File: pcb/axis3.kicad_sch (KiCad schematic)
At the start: 10 parts, among them J13 Mini v1.0 FEMALE sockets, J23 MOTOR PHASES male 1x3, J33 ENCODER JST-SH 6p, J43 MINI POWER: +12V / GND

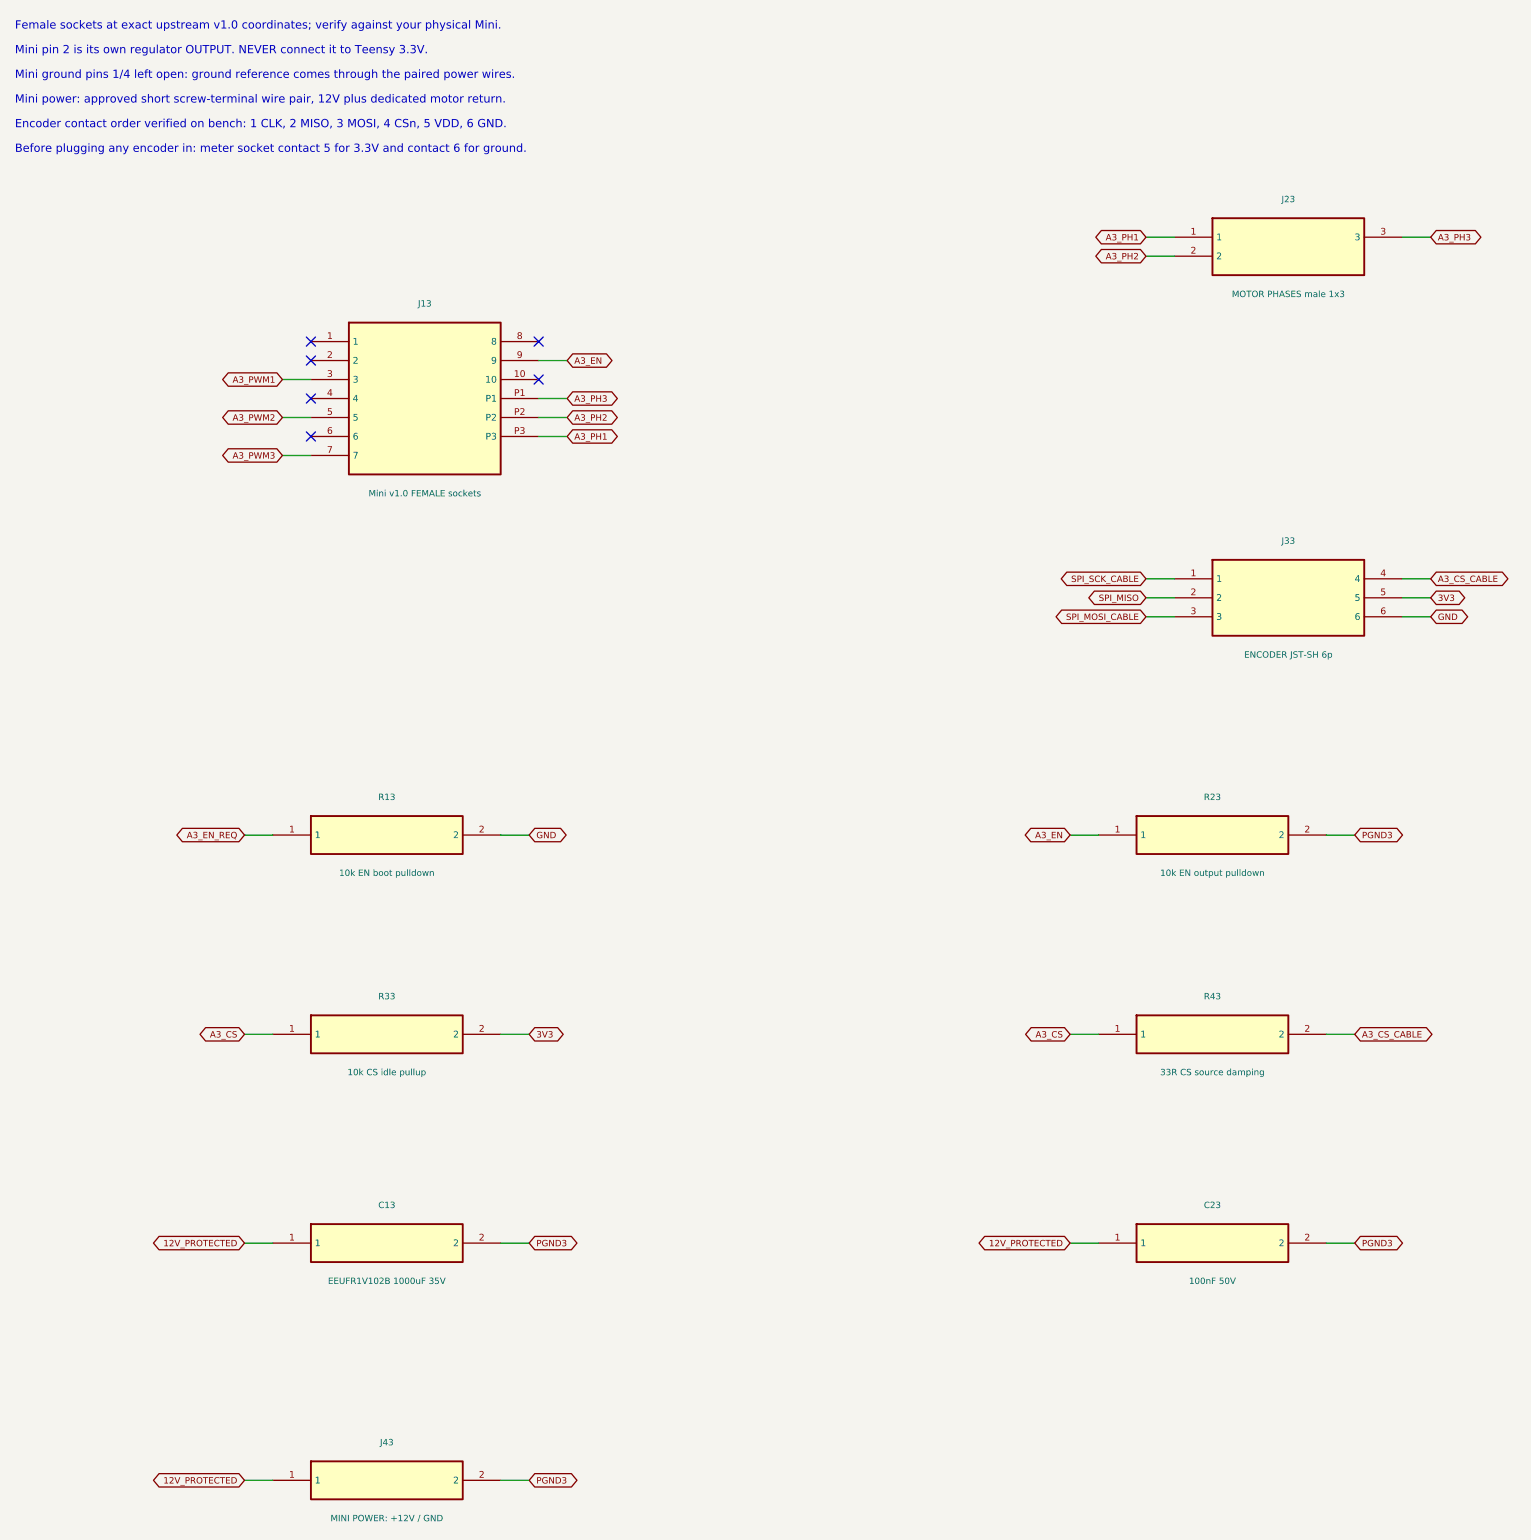
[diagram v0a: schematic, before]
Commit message: feat: finish through-hole six-axis carrier review design
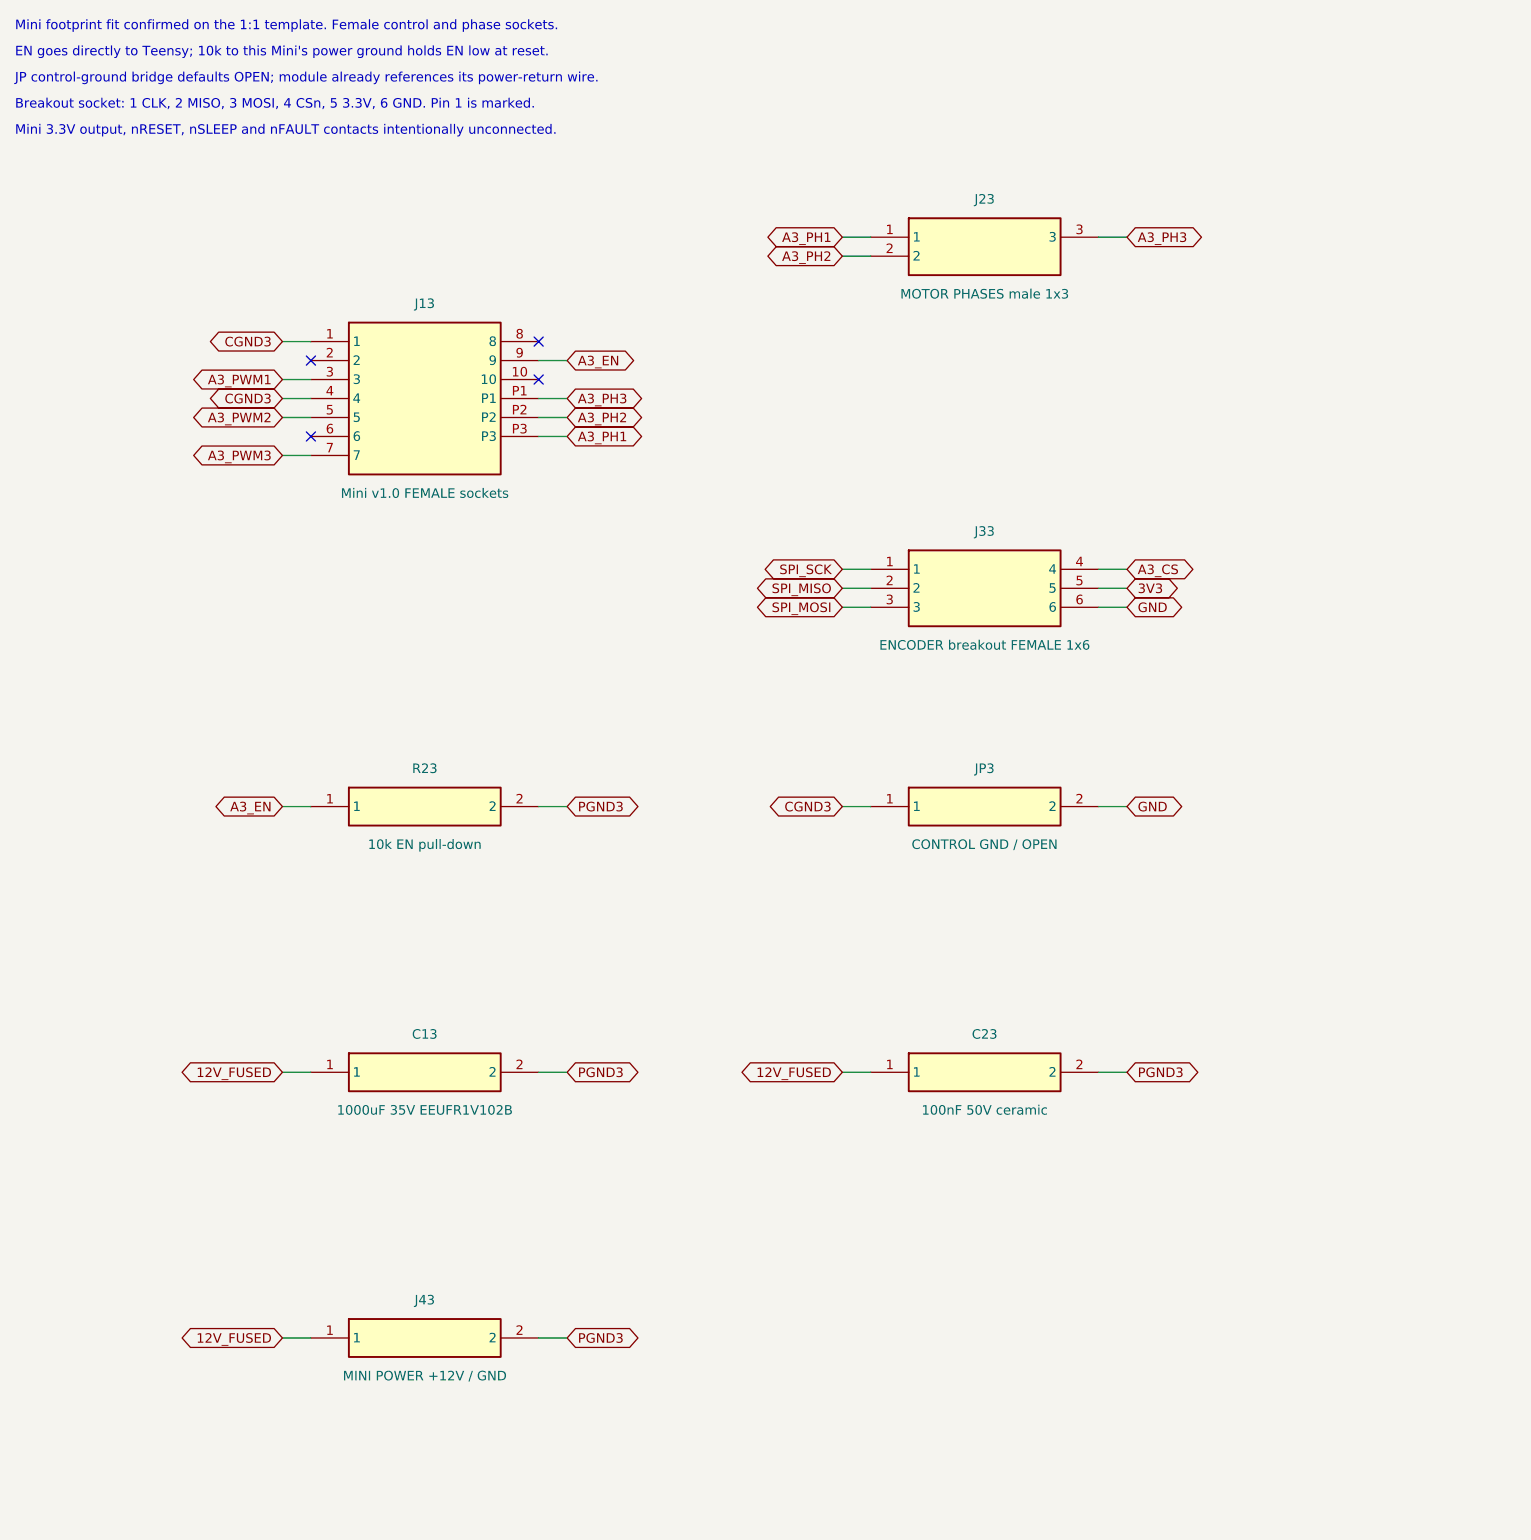
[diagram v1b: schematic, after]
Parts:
- removed R13: 10k EN boot pulldown, Resistor_SMD:R_0603_1608Metric, symbol TrueSkate:R13
- removed R33: 10k CS idle pullup, Resistor_SMD:R_0603_1608Metric, symbol TrueSkate:R33
- removed R43: 33R CS source damping, Resistor_SMD:R_0603_1608Metric, symbol TrueSkate:R43
- added JP3: CONTROL GND / OPEN, TrueSkate:GroundBridge_THT, symbol TrueSkate:JP3
- C13: value EEUFR1V102B 1000uF 35V -> 1000uF 35V EEUFR1V102B; LCSC C128476 -> (none)
- C23: value 100nF 50V -> 100nF 50V ceramic; footprint Capacitor_SMD:C_0603_1608Metric -> Capacitor_THT:C_Disc_D5.0mm_W2.5mm_P5.00mm; LCSC C14663 -> (none)
- J33: value ENCODER JST-SH 6p -> ENCODER breakout FEMALE 1x6; footprint Connector_JST:JST_SH_BM06B-SRSS-TB_1x06-1MP_P1.00mm_Vertical -> Connector_PinSocket_2.54mm:PinSocket_1x06_P2.54mm_Vertical; LCSC C160392 -> (none)
- J43: value MINI POWER: +12V / GND -> MINI POWER +12V / GND
- R23: value 10k EN output pulldown -> 10k EN pull-down; footprint Resistor_SMD:R_0603_1608Metric -> Resistor_THT:R_Axial_DIN0207_L6.3mm_D2.5mm_P7.62mm_Horizontal; LCSC C25804 -> (none)
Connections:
- net A3_CS_CABLE is gone; now on net A3_CS: J33.4
- net GND: now also JP3.2
- net CGND3: now reaches J13.1
- net CGND3: now also J13.4, JP3.1
- net 12V_PROTECTED renamed 12V_FUSED
- net SPI_MOSI_CABLE renamed SPI_MOSI
- net SPI_SCK_CABLE renamed SPI_SCK
- no-connect marks 6 -> 4
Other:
- note added: "Breakout socket: 1 CLK, 2 MISO, 3 MOSI, 4 CSn, 5 3.3V, 6 GND. Pin 1 is marked."
- note added: "EN goes directly to Teensy; 10k to this Mini's power ground holds EN low at reset."
- note added: "JP control-ground bridge defaults OPEN; module already references its power-return wire."
- note added: "Mini 3.3V output, nRESET, nSLEEP and nFAULT contacts intentionally unconnected."
- note added: "Mini footprint fit confirmed on the 1:1 template. Female control and phase sockets."
- note removed: "Before plugging any encoder in: meter socket contact 5 for 3.3V and contact 6 for ground."
- note removed: "Encoder contact order verified on bench: 1 CLK, 2 MISO, 3 MOSI, 4 CSn, 5 VDD, 6 GND."
- note removed: "Female sockets at exact upstream v1.0 coordinates; verify against your physical Mini."
- note removed: "Mini ground pins 1/4 left open: ground reference comes through the paired power wires."
- note removed: "Mini pin 2 is its own regulator OUTPUT. NEVER connect it to Teensy 3.3V."
- note removed: "Mini power: approved short screw-terminal wire pair, 12V plus dedicated motor return."
- title: 05 / Axis 3: index_splay -> 04 / A3: index_splay
- moved on the sheet: C13, C23, J23, J33, J43, R23

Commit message: feat: use exact Mini v1.0 footprints with direct power routing
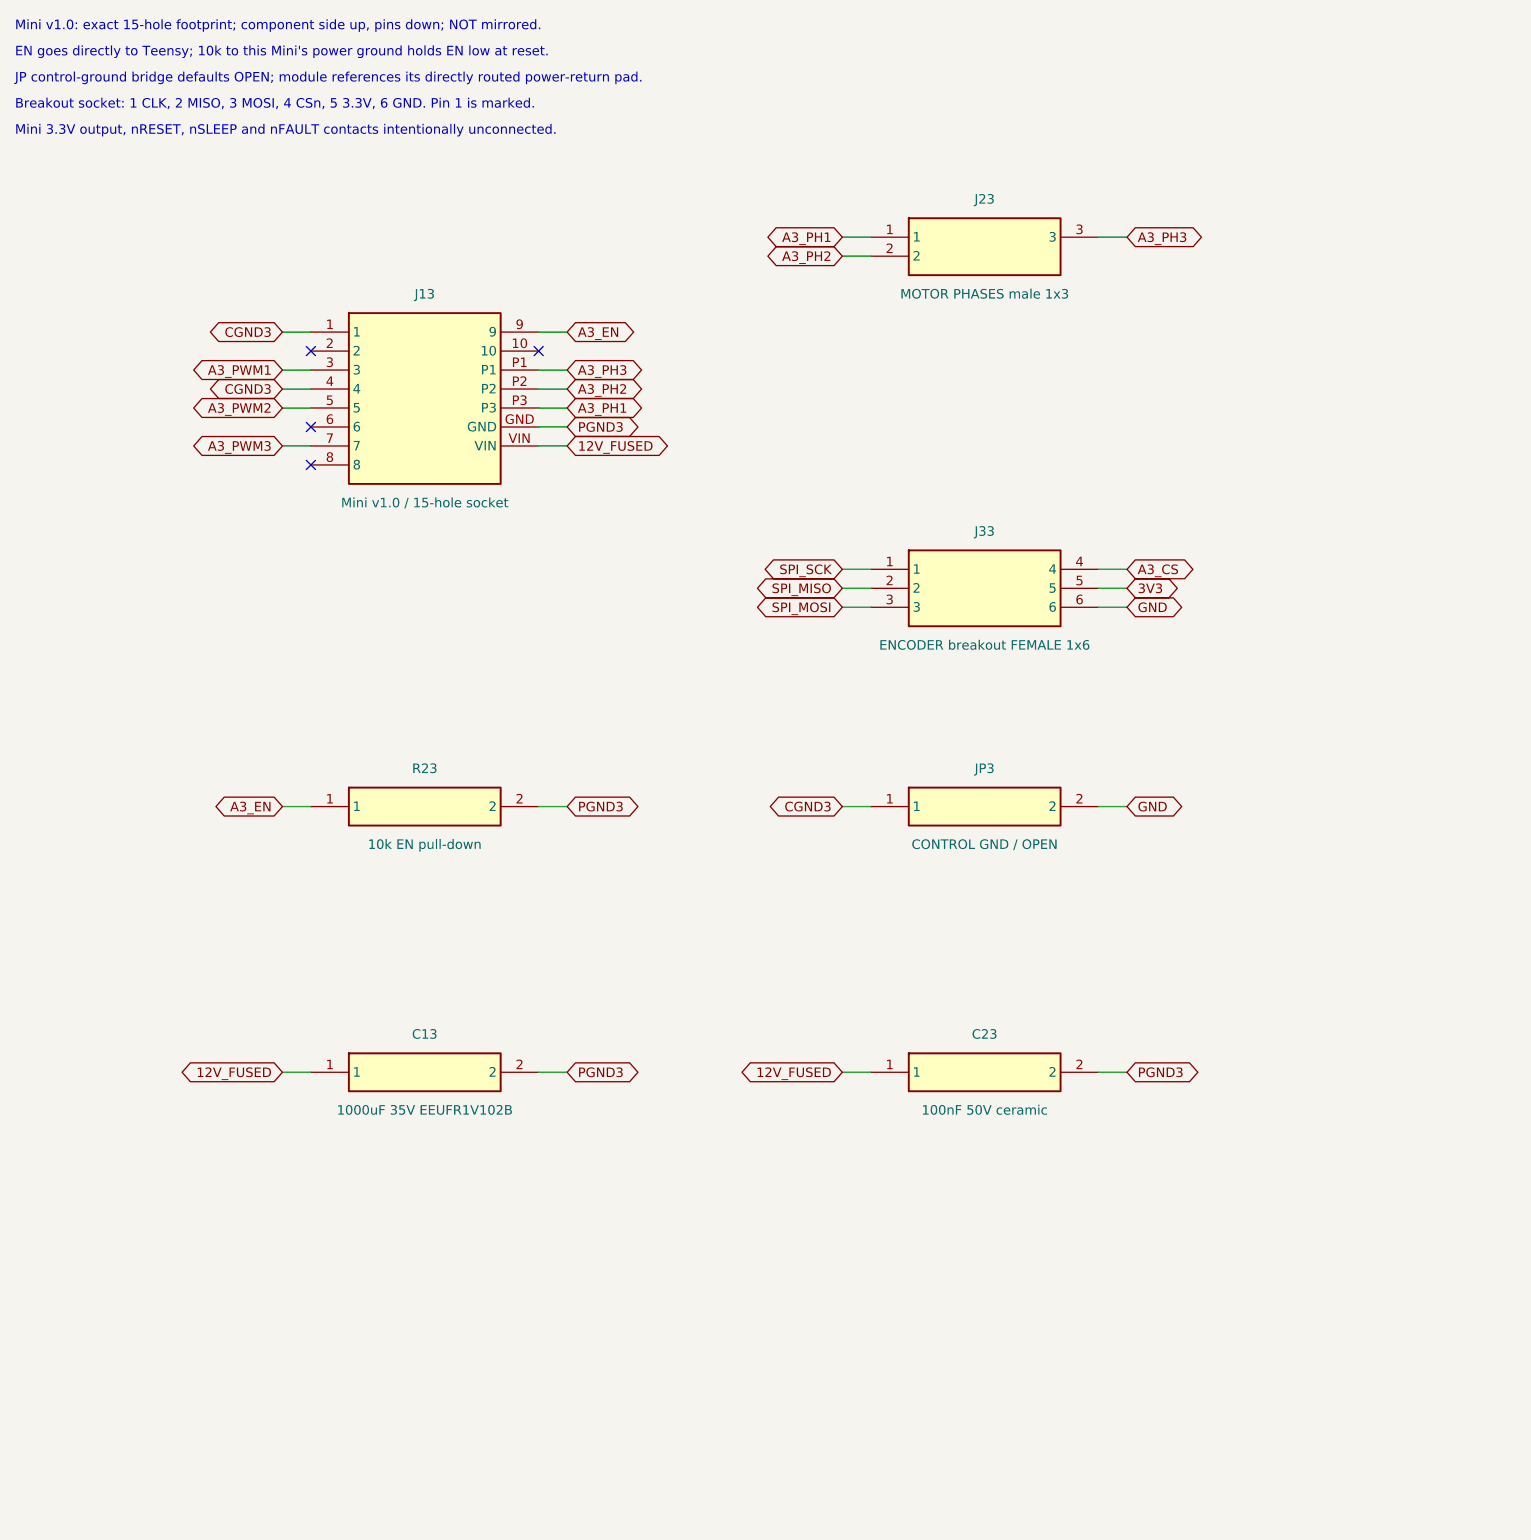
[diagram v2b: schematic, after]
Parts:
- removed J43: MINI POWER +12V / GND, TerminalBlock_Phoenix:TerminalBlock_Phoenix_MKDS-1-2-3.81_1x02_P3.81mm_Horizontal, symbol TrueSkate:J43
- J13: value Mini v1.0 FEMALE sockets -> Mini v1.0 / 15-hole socket; footprint TrueSkate:Mini_v1_Sockets -> TrueSkate:SimpleFOC_Mini_v1.0
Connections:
- net 12V_FUSED: now also J13.VIN
- net PGND3: now also J13.GND
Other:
- note added: "JP control-ground bridge defaults OPEN; module references its directly routed power-return pad."
- note added: "Mini v1.0: exact 15-hole footprint; component side up, pins down; NOT mirrored."
- note removed: "JP control-ground bridge defaults OPEN; module already references its power-return wire."
- note removed: "Mini footprint fit confirmed on the 1:1 template. Female control and phase sockets."

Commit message: feat: relayout carrier with edge connectors and hardware kill
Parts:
- removed JP3: CONTROL GND / OPEN, TrueSkate:GroundBridge_THT, symbol TrueSkate:JP3
- added R33: 10k CS pull-up, TrueSkate:Edge_R_Axial_DIN0207_L6.3mm_D2.5mm_P7.62mm_Horizontal, symbol TrueSkate:R33
- C13: footprint Capacitor_THT:CP_Radial_D12.5mm_P5.00mm -> TrueSkate:Edge_CP_Radial_D12.5mm_P5.00mm
- C23: footprint Capacitor_THT:C_Disc_D5.0mm_W2.5mm_P5.00mm -> TrueSkate:Edge_C_Disc_D5.0mm_W2.5mm_P5.00mm
- J23: footprint Connector_PinHeader_2.54mm:PinHeader_1x03_P2.54mm_Vertical -> TrueSkate:Edge_PinHeader_1x03_P2.54mm_Vertical
- J33: value ENCODER breakout FEMALE 1x6 -> SM06B-SRSS-TB; footprint Connector_PinSocket_2.54mm:PinSocket_1x06_P2.54mm_Vertical -> TrueSkate:Edge_JST_SH_SM06B-SRSS-TB_1x06-1MP_P1.00mm_Horizontal
- R23: footprint Resistor_THT:R_Axial_DIN0207_L6.3mm_D2.5mm_P7.62mm_Horizontal -> TrueSkate:Edge_R_Axial_DIN0207_L6.3mm_D2.5mm_P7.62mm_Horizontal
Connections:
- net CGND3 is gone; now on net GND: J13.1, J13.4
- net PGND3 is gone; now on net GND: C13.2, C23.2, J13.GND, R23.2
- net 3V3: now also R33.2
- net A3_CS: now also R33.1
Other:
- note added: "Entire axis population optional. No shared connection depends on a fitted axis component."
- note added: "Mini v1.0 exact 15-hole footprint, NOT mirrored. Buffered EN with local 10k pull-down."
- note added: "Pin labels derive from design.json encoder_pin_order. CS has an individual 10k pull-up."
- note added: "SH order UNVERIFIED: VERIFY WITH MULTIMETER AGAINST AS5048A BOARD. See README table."
- note removed: "Breakout socket: 1 CLK, 2 MISO, 3 MOSI, 4 CSn, 5 3.3V, 6 GND. Pin 1 is marked."
- note removed: "EN goes directly to Teensy; 10k to this Mini's power ground holds EN low at reset."
- note removed: "JP control-ground bridge defaults OPEN; module references its directly routed power-return pad."
- note removed: "Mini 3.3V output, nRESET, nSLEEP and nFAULT contacts intentionally unconnected."
- note removed: "Mini v1.0: exact 15-hole footprint; component side up, pins down; NOT mirrored."
